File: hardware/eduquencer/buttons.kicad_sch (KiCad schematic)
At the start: 21 parts

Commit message: Hardware: add trigger in&outputs, wire rpi
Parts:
- removed C?: 100n, Capacitor_SMD:C_0603_1608Metric, symbol Device:C
- removed IC?: MCP23018-E_SO, SOIC127P1030X265-28N, symbol MCP23018-E_SO:MCP23018-E_SO
- removed R?: 10k, symbol Device:R_Small
- removed R? (x2): 4k7, symbol Device:R_Small
- added C?: 100n, Capacitor_SMD:C_0603_1608Metric, symbol Device:C
- added IC?: MCP23018-E_SO, SOIC127P1030X265-28N, symbol MCP23018-E_SO:MCP23018-E_SO
- added R? (x2): 4k7, symbol Device:R_Small
- added R?: 10k, symbol Device:R_Small
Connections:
- net +3V3: now also C?.1, IC?.11 (VDD), R?.1, R?.1, R?.1
- net GND: now also C?.2, IC?.1 (VSS), IC?.15 (ADDR)
- net button0: now also IC?.3 (GPB0)
- net button1: now also IC?.4 (GPB1)
- net button10: now also IC?.25 (GPA5)
- net button11: now also IC?.24 (GPA4)
- net button12: now also IC?.23 (GPA3)
- net button13: now also IC?.22 (GPA2)
- net button14: now also IC?.21 (GPA1)
- net button15: now also IC?.20 (GPA0)
- net button2: now also IC?.5 (GPB2)
- net button3: now also IC?.6 (GPB3)
- net button4: now also IC?.7 (GPB4)
- net button5: now also IC?.8 (GPB5)
- net button6: now also IC?.9 (GPB6)
- net button7: now also IC?.10 (GPB7)
- net button8: now also IC?.27 (GPA7)
- net button9: now also IC?.26 (GPA6)
- net scl: now also IC?.12 (SCL), R?.2
- net sda: now also IC?.13 (SDA), R?.2
- new net: IC?.16 (~{RESET}), R?.2

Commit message: Hardware: add test points, tiny cleanup
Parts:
- C?: LCSC C14663 -> (none); LCSC Part # C14663 -> (none)
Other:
- moved on the sheet: SW?

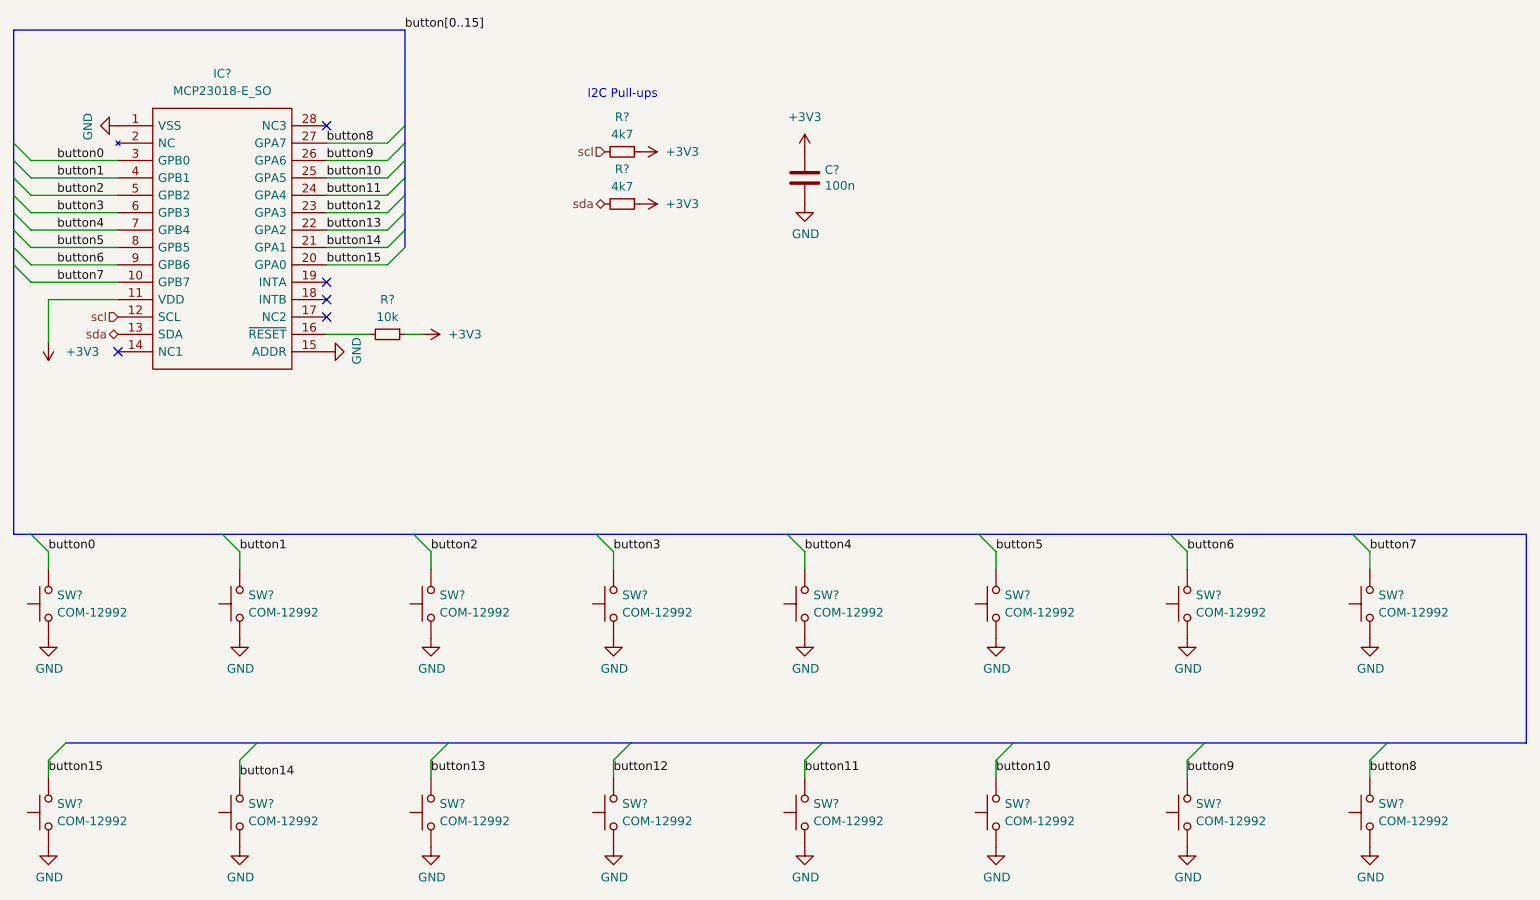
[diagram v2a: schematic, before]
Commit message: Hardware: update models, annotate, fix ERC issues
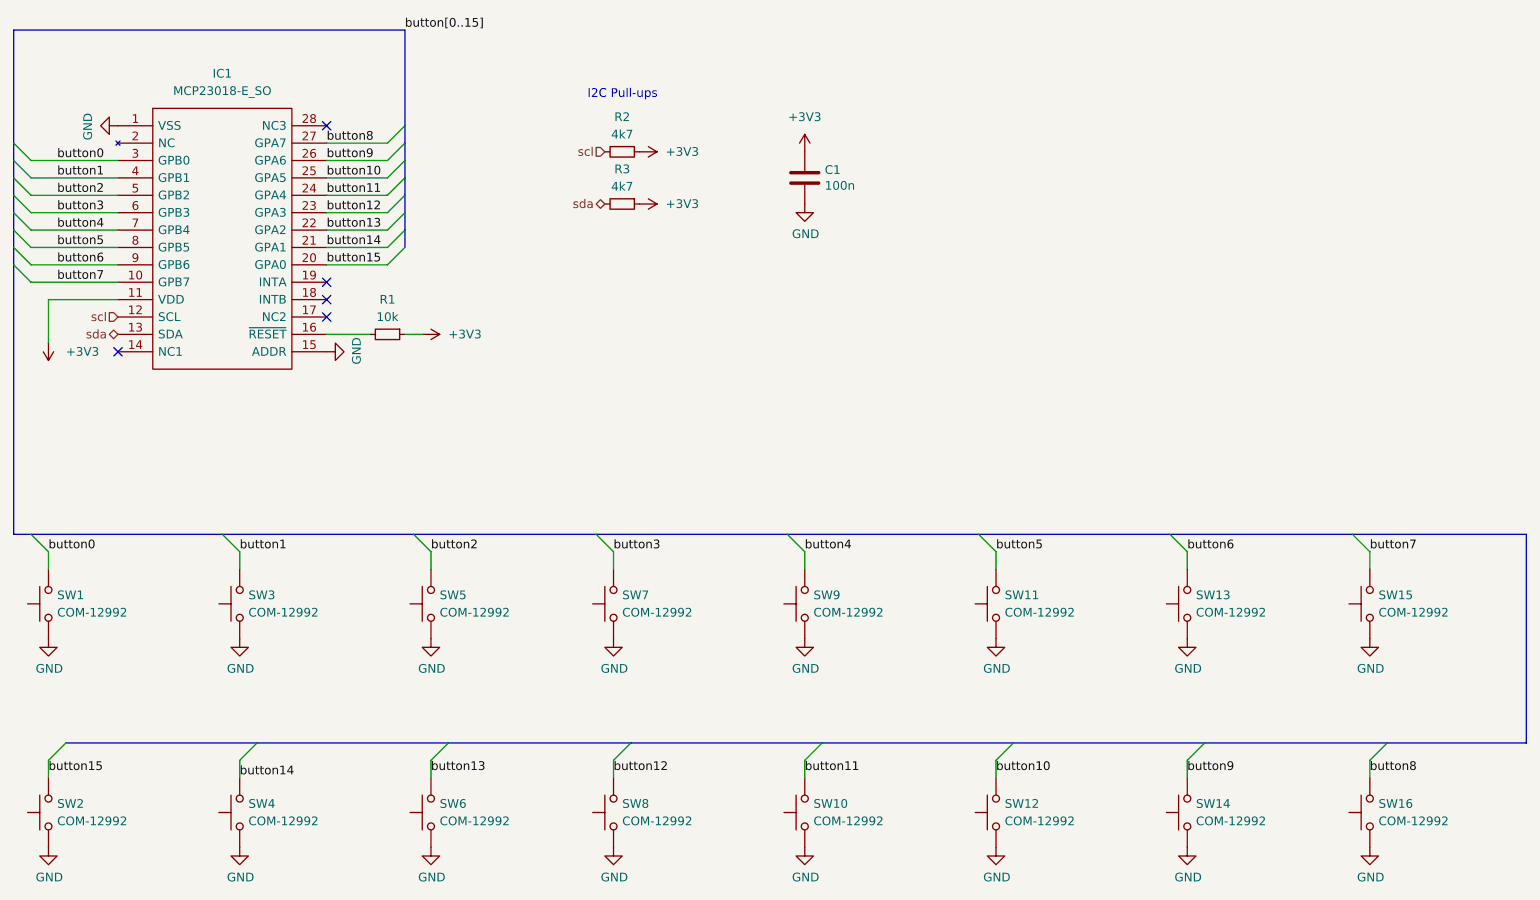
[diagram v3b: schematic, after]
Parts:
- gave numbers to parts that had none: 21
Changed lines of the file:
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@@
   (symbol (lib_id "Device:R_Small") (at 128.27 52.07 270) (unit 1)
     (in_bom yes) (on_board yes)
-    (property "Reference" "R?" (id 0) (at 128.27 46.99 90))
+    (property "Reference" "R3" (id 0) (at 128.27 46.99 90))
     (property "Value" "4k7" (id 1) (at 128.27 49.53 90))
     (property "Footprint" "" (id 2) (at 128.27 52.07 0)
@@
   (symbol (lib_id "Device:R_Small") (at 128.27 44.45 270) (unit 1)
     (in_bom yes) (on_board yes)
-    (property "Reference" "R?" (id 0) (at 128.27 39.37 90))
+    (property "Reference" "R2" (id 0) (at 128.27 39.37 90))
     (property "Value" "4k7" (id 1) (at 128.27 41.91 90))
     (property "Footprint" "" (id 2) (at 128.27 44.45 0)
@@
   (symbol (lib_id "Switch:SW_Push") (at 100.33 140.97 90) (unit 1)
     (in_bom yes) (on_board yes) (fields_autoplaced)
-    (property "Reference" "SW?" (id 0) (at 101.6 139.6999 90)
+    (property "Reference" "SW6" (id 0) (at 101.6 139.6999 90)
       (effects (font (size 1.27 1.27)) (justify right))
     )
@@
   (symbol (lib_id "Switch:SW_Push") (at 100.33 110.49 90) (unit 1)
     (in_bom yes) (on_board yes) (fields_autoplaced)
-    (property "Reference" "SW?" (id 0) (at 101.6 109.2199 90)
+    (property "Reference" "SW5" (id 0) (at 101.6 109.2199 90)
       (effects (font (size 1.27 1.27)) (justify right))
     )
@@
   (symbol (lib_id "Device:C") (at 154.94 48.26 0) (unit 1)
     (in_bom yes) (on_board yes)
-    (property "Reference" "C?" (id 0) (at 157.861 47.0916 0)
+    (property "Reference" "C1" (id 0) (at 157.861 47.0916 0)
       (effects (font (size 1.27 1.27)) (justify left))
     )
@@
   (symbol (lib_id "MCP23018-E_SO:MCP23018-E_SO") (at 54.61 40.64 0) (unit 1)
     (in_bom yes) (on_board yes) (fields_autoplaced)
-    (property "Reference" "IC?" (id 0) (at 69.85 33.02 0))
+    (property "Reference" "IC1" (id 0) (at 69.85 33.02 0))
     (property "Value" "MCP23018-E_SO" (id 1) (at 69.85 35.56 0))
     (property "Footprint" "SOIC127P1030X265-28N" (id 2) (at 81.28 38.1 0)
@@
   (symbol (lib_id "Switch:SW_Push") (at 154.94 140.97 90) (unit 1)
     (in_bom yes) (on_board yes) (fields_autoplaced)
-    (property "Reference" "SW?" (id 0) (at 156.21 139.6999 90)
+    (property "Reference" "SW10" (id 0) (at 156.21 139.6999 90)
       (effects (font (size 1.27 1.27)) (justify right))
     )
@@
   (symbol (lib_id "Switch:SW_Push") (at 44.45 140.97 90) (unit 1)
     (in_bom yes) (on_board yes) (fields_autoplaced)
-    (property "Reference" "SW?" (id 0) (at 45.72 139.6999 90)
+    (property "Reference" "SW2" (id 0) (at 45.72 139.6999 90)
       (effects (font (size 1.27 1.27)) (justify right))
     )
@@
   (symbol (lib_id "Switch:SW_Push") (at 237.49 140.97 90) (unit 1)
     (in_bom yes) (on_board yes) (fields_autoplaced)
-    (property "Reference" "SW?" (id 0) (at 238.76 139.6999 90)
+    (property "Reference" "SW16" (id 0) (at 238.76 139.6999 90)
       (effects (font (size 1.27 1.27)) (justify right))
     )
@@
   (symbol (lib_id "Switch:SW_Push") (at 127 110.49 90) (unit 1)
     (in_bom yes) (on_board yes) (fields_autoplaced)
-    (property "Reference" "SW?" (id 0) (at 128.27 109.2199 90)
+    (property "Reference" "SW7" (id 0) (at 128.27 109.2199 90)
       (effects (font (size 1.27 1.27)) (justify right))
     )
@@
   (symbol (lib_id "Switch:SW_Push") (at 154.94 110.49 90) (unit 1)
     (in_bom yes) (on_board yes) (fields_autoplaced)
-    (property "Reference" "SW?" (id 0) (at 156.21 109.2199 90)
+    (property "Reference" "SW9" (id 0) (at 156.21 109.2199 90)
       (effects (font (size 1.27 1.27)) (justify right))
     )
@@
   (symbol (lib_id "Switch:SW_Push") (at 44.45 110.49 90) (unit 1)
     (in_bom yes) (on_board yes) (fields_autoplaced)
-    (property "Reference" "SW?" (id 0) (at 45.72 109.2199 90)
+    (property "Reference" "SW1" (id 0) (at 45.72 109.2199 90)
       (effects (font (size 1.27 1.27)) (justify right))
     )
@@
   (symbol (lib_id "Switch:SW_Push") (at 210.82 140.97 90) (unit 1)
     (in_bom yes) (on_board yes) (fields_autoplaced)
-    (property "Reference" "SW?" (id 0) (at 212.09 139.6999 90)
+    (property "Reference" "SW14" (id 0) (at 212.09 139.6999 90)
       (effects (font (size 1.27 1.27)) (justify right))
     )
@@
   (symbol (lib_id "Device:R_Small") (at 93.98 71.12 270) (unit 1)
     (in_bom yes) (on_board yes)
-    (property "Reference" "R?" (id 0) (at 93.98 66.04 90))
+    (property "Reference" "R1" (id 0) (at 93.98 66.04 90))
     (property "Value" "10k" (id 1) (at 93.98 68.58 90))
     (property "Footprint" "" (id 2) (at 93.98 71.12 0)
@@
   (symbol (lib_id "Switch:SW_Push") (at 237.49 110.49 90) (unit 1)
     (in_bom yes) (on_board yes) (fields_autoplaced)
-    (property "Reference" "SW?" (id 0) (at 238.76 109.2199 90)
+    (property "Reference" "SW15" (id 0) (at 238.76 109.2199 90)
       (effects (font (size 1.27 1.27)) (justify right))
     )
@@
   (symbol (lib_id "Switch:SW_Push") (at 72.39 140.97 90) (unit 1)
     (in_bom yes) (on_board yes) (fields_autoplaced)
-    (property "Reference" "SW?" (id 0) (at 73.66 139.6999 90)
+    (property "Reference" "SW4" (id 0) (at 73.66 139.6999 90)
       (effects (font (size 1.27 1.27)) (justify right))
     )
@@
   (symbol (lib_id "Switch:SW_Push") (at 210.82 110.49 90) (unit 1)
     (in_bom yes) (on_board yes) (fields_autoplaced)
-    (property "Reference" "SW?" (id 0) (at 212.09 109.2199 90)
+    (property "Reference" "SW13" (id 0) (at 212.09 109.2199 90)
       (effects (font (size 1.27 1.27)) (justify right))
     )
@@
   (symbol (lib_id "Switch:SW_Push") (at 182.88 140.97 90) (unit 1)
     (in_bom yes) (on_board yes) (fields_autoplaced)
-    (property "Reference" "SW?" (id 0) (at 184.15 139.6999 90)
+    (property "Reference" "SW12" (id 0) (at 184.15 139.6999 90)
       (effects (font (size 1.27 1.27)) (justify right))
     )
@@
   (symbol (lib_id "Switch:SW_Push") (at 127 140.97 90) (unit 1)
     (in_bom yes) (on_board yes) (fields_autoplaced)
-    (property "Reference" "SW?" (id 0) (at 128.27 139.6999 90)
+    (property "Reference" "SW8" (id 0) (at 128.27 139.6999 90)
       (effects (font (size 1.27 1.27)) (justify right))
     )
@@
   (symbol (lib_id "Switch:SW_Push") (at 182.88 110.49 90) (unit 1)
     (in_bom yes) (on_board yes) (fields_autoplaced)
-    (property "Reference" "SW?" (id 0) (at 184.15 109.2199 90)
+    (property "Reference" "SW11" (id 0) (at 184.15 109.2199 90)
       (effects (font (size 1.27 1.27)) (justify right))
     )
@@
   (symbol (lib_id "Switch:SW_Push") (at 72.39 110.49 90) (unit 1)
     (in_bom yes) (on_board yes) (fields_autoplaced)
-    (property "Reference" "SW?" (id 0) (at 73.66 109.2199 90)
-      (effects (font (size 1.27 1.27)) (justify right))
-    )
+    (property "Reference" "SW3" (id 0) (at 73.66 109.2199 90)
+      (effects (font (size 1.27 1.27)) (justify right))
+    )

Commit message: Hardware: assign all footprints
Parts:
- C1: footprint Capacitor_SMD:C_0603_1608Metric -> Capacitor_SMD:C_0603_1608Metric_Pad1.08x0.95mm_HandSolder
- IC1: footprint SOIC127P1030X265-28N -> MCP23018-E_SO:SOIC127P1030X265-28N
- R1, R2, R3: footprint (none) -> Resistor_SMD:R_0603_1608Metric_Pad0.98x0.95mm_HandSolder
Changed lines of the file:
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@@
     (property "Reference" "R3" (id 0) (at 128.27 46.99 90))
     (property "Value" "4k7" (id 1) (at 128.27 49.53 90))
-    (property "Footprint" "" (id 2) (at 128.27 52.07 0)
+    (property "Footprint" "Resistor_SMD:R_0603_1608Metric_Pad0.98x0.95mm_HandSolder" (id 2) (at 128.27 52.07 0)
       (effects (font (size 1.27 1.27)) hide)
     )
@@
     (property "Reference" "R2" (id 0) (at 128.27 39.37 90))
     (property "Value" "4k7" (id 1) (at 128.27 41.91 90))
-    (property "Footprint" "" (id 2) (at 128.27 44.45 0)
+    (property "Footprint" "Resistor_SMD:R_0603_1608Metric_Pad0.98x0.95mm_HandSolder" (id 2) (at 128.27 44.45 0)
       (effects (font (size 1.27 1.27)) hide)
     )
@@
       (effects (font (size 1.27 1.27)) (justify left))
     )
-    (property "Footprint" "Capacitor_SMD:C_0603_1608Metric" (id 2) (at 155.9052 52.07 0)
+    (property "Footprint" "Capacitor_SMD:C_0603_1608Metric_Pad1.08x0.95mm_HandSolder" (id 2) (at 155.9052 52.07 0)
       (effects (font (size 1.27 1.27)) hide)
     )
@@
     (property "Reference" "IC1" (id 0) (at 69.85 33.02 0))
     (property "Value" "MCP23018-E_SO" (id 1) (at 69.85 35.56 0))
-    (property "Footprint" "SOIC127P1030X265-28N" (id 2) (at 81.28 38.1 0)
+    (property "Footprint" "MCP23018-E_SO:SOIC127P1030X265-28N" (id 2) (at 81.28 38.1 0)
       (effects (font (size 1.27 1.27)) (justify left) hide)
     )
@@
     (property "Reference" "R1" (id 0) (at 93.98 66.04 90))
     (property "Value" "10k" (id 1) (at 93.98 68.58 90))
-    (property "Footprint" "" (id 2) (at 93.98 71.12 0)
-      (effects (font (size 1.27 1.27)) hide)
-    )
+    (property "Footprint" "Resistor_SMD:R_0603_1608Metric_Pad0.98x0.95mm_HandSolder" (id 2) (at 93.98 71.12 0)
+      (effects (font (size 1.27 1.27)) hide)
+    )
